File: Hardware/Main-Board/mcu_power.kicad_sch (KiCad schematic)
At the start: 4 parts

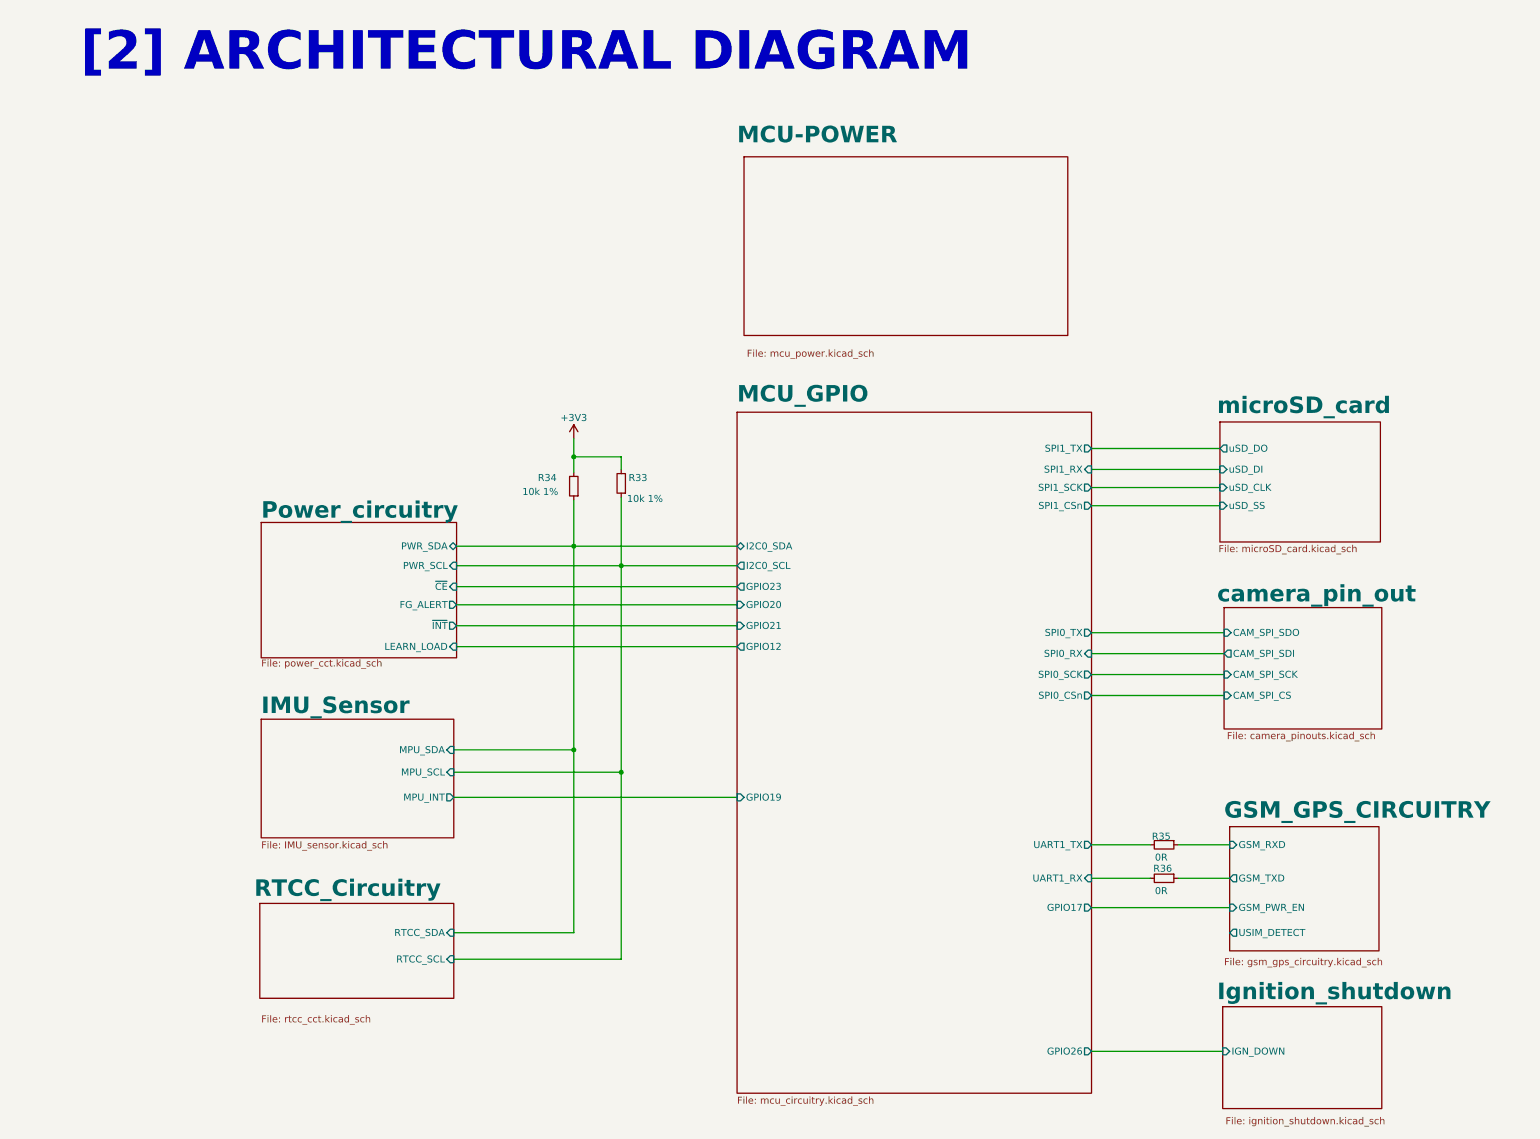
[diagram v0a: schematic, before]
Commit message: Done with main board design, and camera interconnect in progress
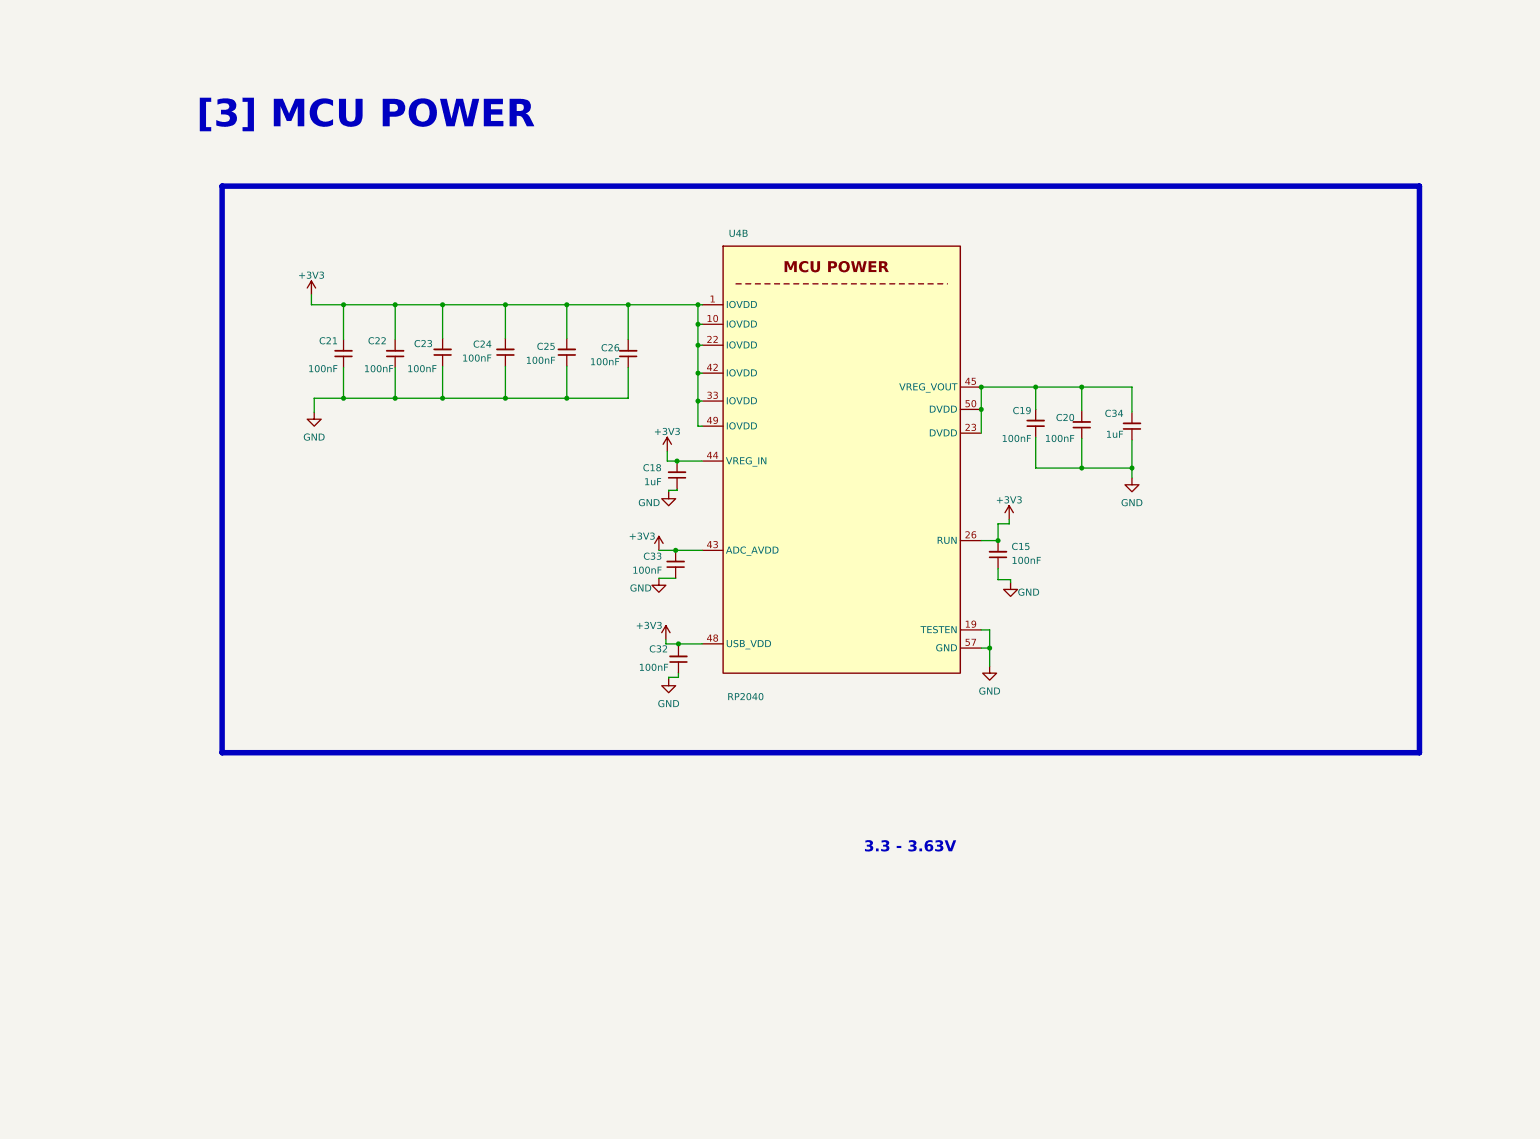
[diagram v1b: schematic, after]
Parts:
- removed R33, R34: 10k 1%, Resistor_SMD:R_0402_1005Metric, symbol Device:R_Small
- removed R35, R36: 0R, Resistor_SMD:R_0402_1005Metric, symbol Device:R_Small
- added C15, C19, C20, C21, C22, C23, C24, C25, C26, C32, C33: 100nF, Capacitor_SMD:C_0402_1005Metric, symbol Device:C_Small
- added C18, C34: 1uF, Capacitor_SMD:C_0402_1005Metric, symbol Device:C_Small
- added U4: RP2040, Package_DFN_QFN:QFN-56-1EP_7x7mm_P0.4mm_EP3.2x3.2mm, symbol MCU_RaspberryPi:RP2040
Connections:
- net +3V3: now also C15.2, C18.2, C21.2, C22.2, C23.2, C24.2, C25.2, C26.2, C32.2, C33.2, U4.1 (IOVDD), U4.10 (IOVDD), U4.22 (IOVDD), U4.26 (RUN), U4.33 (IOVDD), U4.42 (IOVDD), U4.43 (ADC_AVDD), U4.44 (VREG_IN), U4.48 (USB_VDD), U4.49 (IOVDD)
- new net: C19.2, C20.2, C34.2, U4.23 (DVDD), U4.45 (VREG_VOUT), U4.50 (DVDD)
- new net GND: C15.1, C18.1, C19.1, C20.1, C21.1, C22.1, C23.1, C24.1, C25.1, C26.1, C32.1, C33.1, C34.1, U4.19 (TESTEN), U4.57 (GND)
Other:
- removed sheet GSM_GPS_CIRCUITRY
- removed sheet IMU_Sensor
- removed sheet Ignition_shutdown
- removed sheet MCU-POWER
- removed sheet MCU_GPIO
- removed sheet Power_circuitry
- removed sheet RTCC_Circuitry
- removed sheet camera_pin_out
- removed sheet microSD_card
- note added: "3.3 - 3.63V"
- note added: "[3] MCU POWER"
- note removed: "[2] ARCHITECTURAL DIAGRAM"
